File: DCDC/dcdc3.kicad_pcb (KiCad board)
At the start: 2 copper layers, 90 x 90 mm, 83 parts, among them M1-1 30V 60A, M1-2 30V 60A, M1-3 30V 60A, M2-1 30V 35A, M2-2 30V 35A, M2-3 30V 35A

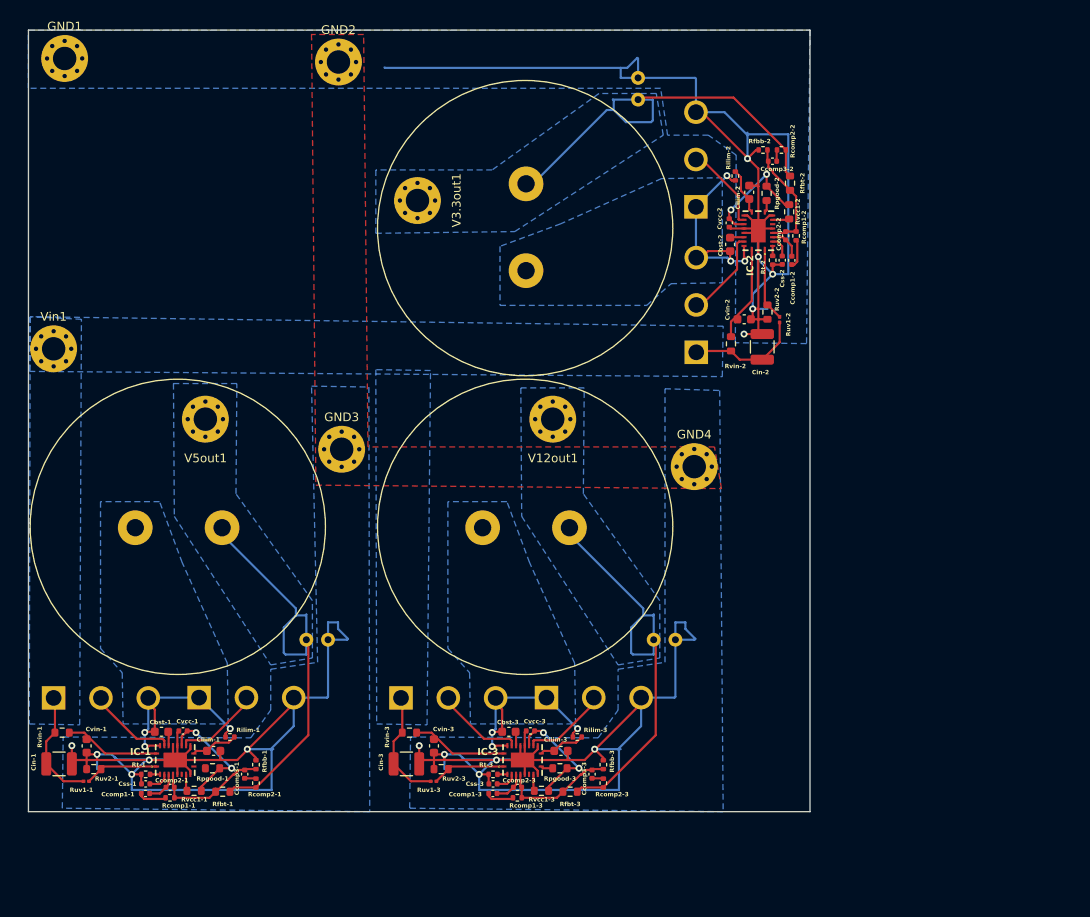
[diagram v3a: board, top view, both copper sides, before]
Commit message: pcb designed for 3 outputs
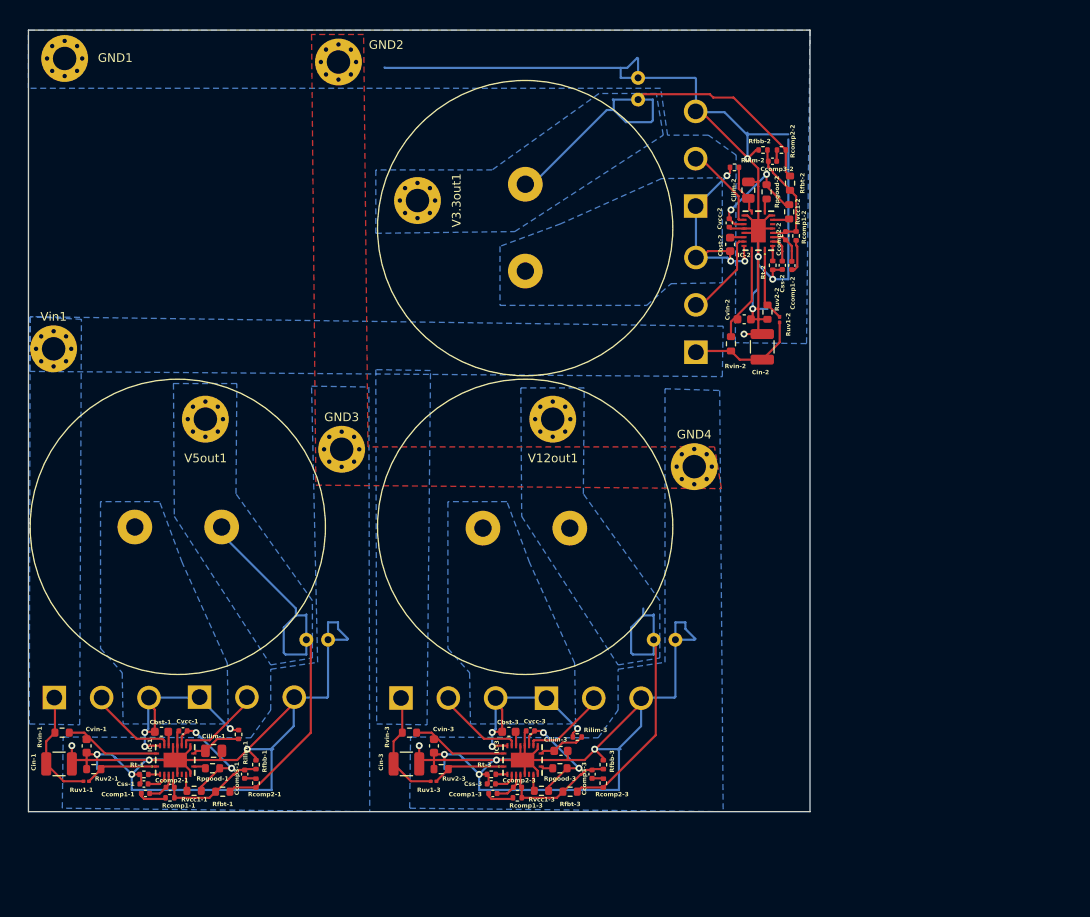
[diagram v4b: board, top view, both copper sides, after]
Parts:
- Ccomp1-1, Ccomp1-2: value 15 nF -> 8.2n
- Ccomp2-1: value 1.2 n -> 820p
- Ccomp2-2: value 1.2 n -> 1 n
- Ccomp3-1: value 910 p -> 470 p
- Ccomp3-2: value 910 p -> 330p
- Cilim-1, Cilim-2: value 10 p -> 5.1p; footprint Capacitor_SMD:C_0603_1608Metric -> Capacitor_SMD:C_0805_2012Metric
- Cout-1, Cout-2: value 56 u -> 10u
- L1-1: value 4.7 u -> 3.3u
- L1-2: value 4.7 u -> 2.2u
- Rcomp1-1: value 1.78 k -> 1.54k
- Rcomp1-2: value 1.78 k -> 1.27k
- Rcomp2-1: value 1.82 k -> 162
- Rcomp2-2: value 1.82 k -> 237
- Rfbb-1: value 1.27 k -> 3.4k
- Rfbb-2: value 1.27 k -> 5.76k
- Rilim-1: value 619 -> 1.74k
- Rilim-2: value 619 -> 1.5k
- Rt-1, Rt-2: value 69.8k -> 39.2k
- moved Rilim-1 1.04 mm to (54.2, 121.1), turned to 90 degrees
- moved Rilim-2 1.00 mm to (111.3, 55.8), turned to 180 degrees
- moved Ccomp1-2 0.59 mm to (117.9, 67.1)
- moved Css-2 0.59 mm to (116.8, 67.1)
- moved Rt-2 0.59 mm to (115.7, 67.1)
- moved Cilim-2 0.26 mm to (112.9, 58.4)
- moved Css-1 0.20 mm to (43.3, 126.8)
- moved Rt-1 0.20 mm to (43.3, 125.7)
- moved Css-3 0.20 mm to (83.3, 126.8)
- moved Rt-3 0.20 mm to (83.3, 125.7)
- moved Rpgood-2 0.17 mm to (115.0, 58.6)
- moved M2-2 0.10 mm to (106.8, 60.3)
- moved L1-1 0.09 mm to (47.2, 97.2)
- moved L1-2 0.09 mm to (87.2, 62.8)
- moved M1-1 0.09 mm to (33.0, 116.9)
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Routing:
- net /12V/V12out: track 50.2 -> 37.0 mm
- net /12V/GND: track 381.1 -> 378.6 mm
- net Net-(IC-1-PGOOD): track 0.00 -> 1.41 mm
- net Net-(Ccomp1-2-Pad1): track 3.29 -> 4.07 mm
- net Net-(IC-2-SS/TRK): track 2.46 -> 3.05 mm
- net Net-(IC-2-RT): track 1.14 -> 1.73 mm
- net Net-(IC-2-COMP): track 3.80 -> 4.39 mm
- net Net-(IC-1-ILIM): track 5.45 -> 6.02 mm

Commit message: one module of the dcdc converter seems ready again...
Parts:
- removed Cbst-2, Cbst-3: 100 n, Capacitor_SMD:C_0603_1608Metric
- removed Ccomp1-2: 8.2n, Capacitor_SMD:C_0402_1005Metric
- removed Ccomp1-3: 15 nF, Capacitor_SMD:C_0402_1005Metric
- removed Ccomp2-2: 1 n, Capacitor_SMD:C_0402_1005Metric
- removed Ccomp2-3: 1.2 n, Capacitor_SMD:C_0402_1005Metric
- removed Ccomp3-2: 330p, Capacitor_SMD:C_0402_1005Metric
- removed Ccomp3-3: 910 p, Capacitor_SMD:C_0402_1005Metric
- removed Cilim-2: 5.1p, Capacitor_SMD:C_0805_2012Metric
- removed Cilim-3: 10 p, Capacitor_SMD:C_0603_1608Metric
- removed Cin-2, Cin-3: 4.7 uF, Capacitor_SMD:C_1210_3225Metric
- removed Cout-2: 10u, Capacitor_THT:C_Radial_D6.3mm_H5.0mm_P2.50mm
- removed Cout-3: 56 u, Capacitor_THT:C_Radial_D6.3mm_H5.0mm_P2.50mm
- removed Css-2, Css-3: 56n, Capacitor_SMD:C_0402_1005Metric
- removed Cvcc-2, Cvcc-3: 2.2 u, Capacitor_SMD:C_0402_1005Metric
- removed Cvin-2, Cvin-3: 100 nF, Capacitor_SMD:C_0603_1608Metric
- removed GND2, GND3, GND4, V12out1, V3.3out1: ~, MountingHole:MountingHole_2.7mm_M2.5_Pad_Via
- removed IC-1, IC-2, IC-3: LM5145RGYR, Library:RGY0020B
- removed L1-2: 2.2u, Library:A3mmCoil
- removed L1-3: 4.7 u, Library:A3mmCoil
- removed M1-2, M1-3: 30V 60A, Library:TO545P521X1594X2566-3P
- removed M2-2, M2-3: 30V 35A, Library:TO545P521X1594X2566-3P
- removed Rcomp1-2: 1.27k, Resistor_SMD:R_0402_1005Metric
- removed Rcomp1-3: 1.78 k, Resistor_SMD:R_0402_1005Metric
- removed Rcomp2-2: 237, Resistor_SMD:R_0402_1005Metric
- removed Rcomp2-3: 1.82 k, Resistor_SMD:R_0402_1005Metric
- removed Rfbb-2: 5.76k, Resistor_SMD:R_0402_1005Metric
- removed Rfbb-3: 1.27 k, Resistor_SMD:R_0402_1005Metric
- removed Rfbt-2, Rfbt-3: 18 k, Resistor_SMD:R_0603_1608Metric
- removed Rilim-2: 1.5k, Resistor_SMD:R_0402_1005Metric
- removed Rilim-3: 619, Resistor_SMD:R_0402_1005Metric
- removed Rpgood-2, Rpgood-3, Rvcc1-2, Rvcc1-3: 20 k, Resistor_SMD:R_0603_1608Metric
- removed Rt-2: 39.2k, Resistor_SMD:R_0402_1005Metric
- removed Rt-3: 69.8k, Resistor_SMD:R_0402_1005Metric
- removed Ruv1-2, Ruv1-3: 68.1k, Resistor_SMD:R_0201_0603Metric
- removed Ruv2-2, Ruv2-3: 9.1 k, Resistor_SMD:R_0603_1608Metric
- removed Rvin-2, Rvin-3: 2.1, Resistor_SMD:R_0603_1608Metric
- removed Vin1: 12.5-22V, MountingHole:MountingHole_2.7mm_M2.5_Pad_Via
- added U1: LM5145RGYR, Library:RGY0020B, F.Cu at (76.5, 135.1)
- moved GND1 86.9 mm to (95.4, 104.9)
- moved Ccomp1-1 41.0 mm to (82.9, 139.3), turned to 180 degrees
- moved V5out1 40.5 mm to (85.5, 105.0)
- moved Cilim-1 38.0 mm to (88.3, 131.6)
- moved Rvin-1 38.0 mm to (69.9, 132.9)
- moved Rcomp1-1 37.8 mm to (82.8, 138.1), turned to 0 degrees
- moved Cout-1 37.2 mm to (97.7, 120.8), turned to 180 degrees
- moved Cvin-1 35.6 mm to (70.2, 134.5), turned to 0 degrees
- moved Ruv1-1 35.3 mm to (70.6, 135.9)
- moved Rfbt-1 35.2 mm to (87.1, 133.9)
- moved Cin-1 35.0 mm to (66.6, 135.8), turned to -90 degrees
- moved Ruv2-1 34.4 mm to (69.2, 138.4), turned to -90 degrees
- moved L1-1 34.3 mm to (78.0, 112.5)
- moved Rcomp2-1 33.3 mm to (87.9, 137.1), turned to -90 degrees
- moved Rpgood-1 33.1 mm to (82.6, 135.4), turned to -90 degrees
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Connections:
- Cbst-1 pad 2: Net-(IC-1-SW) -> Net-(U1-SW)
- L1-1 pad 1: Net-(IC-1-SW) -> Net-(U1-SW)
- M1-1 pad 1: /12V/Vin -> Net-(U1-HO)
- M1-1 pad 2: Net-(IC-1-HO) -> /12V/Vin
- M1-1 pad 3: Net-(IC-1-SW) -> Net-(U1-SW)
- M2-1 pad 1: Net-(IC-1-SW) -> Net-(U1-LO)
- M2-1 pad 2: Net-(IC-1-LO) -> Net-(U1-SW)
- Rilim-1 pad 2: Net-(IC-1-SW) -> Net-(U1-SW)
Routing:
- net /12V/GND: track 378.6 -> 70.2 mm, vias 15 -> 4
- net /3.3V/V3.3out: track 50.5 -> 0.00 mm
- net Net-(U1-SW): track 0.00 -> 46.4 mm
- net /12V/V12out: track 37.0 -> 0.00 mm
- net Net-(IC-3-SW): track 24.3 -> 0.00 mm, vias 3 -> 0
- net Net-(IC-2-SW): track 24.2 -> 0.00 mm, vias 3 -> 0
- net Net-(IC-1-SW): track 24.1 -> 0.00 mm, vias 3 -> 0
- net Net-(U1-HO): track 0.00 -> 18.6 mm, vias 0 -> 3
- net Net-(IC-2-FB): track 13.9 -> 0.00 mm
- net Net-(IC-3-FB): track 13.9 -> 0.00 mm
- net Net-(IC-2-VCC): track 13.5 -> 0.00 mm, vias 2 -> 0
- net Net-(IC-3-VCC): track 13.5 -> 0.00 mm, vias 2 -> 0
- net Net-(M1-3-D): track 13.2 -> 0.00 mm
- net /12V/Vin: track 26.4 -> 14.8 mm
- net Net-(IC-3-VIN): track 11.0 -> 0.00 mm
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- added copper zone on F.Cu, net /12V/Vin
- added copper zone on F.Cu, net /5V/V5out
- added copper zone on F.Cu, net Net-(U1-SW)
- removed copper zone on B.Cu, net /12V/V12out
- removed copper zone on B.Cu, net /12V/Vin
- removed copper zone on B.Cu, net /3.3V/V3.3out
- removed copper zone on B.Cu, net /5V/V5out
- removed copper zone on B.Cu, net Net-(IC-1-SW)
- removed copper zone on B.Cu, net Net-(IC-2-SW)
- removed copper zone on B.Cu, net Net-(IC-3-SW)
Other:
- board size 90 x 90 mm -> 40 x 40 mm

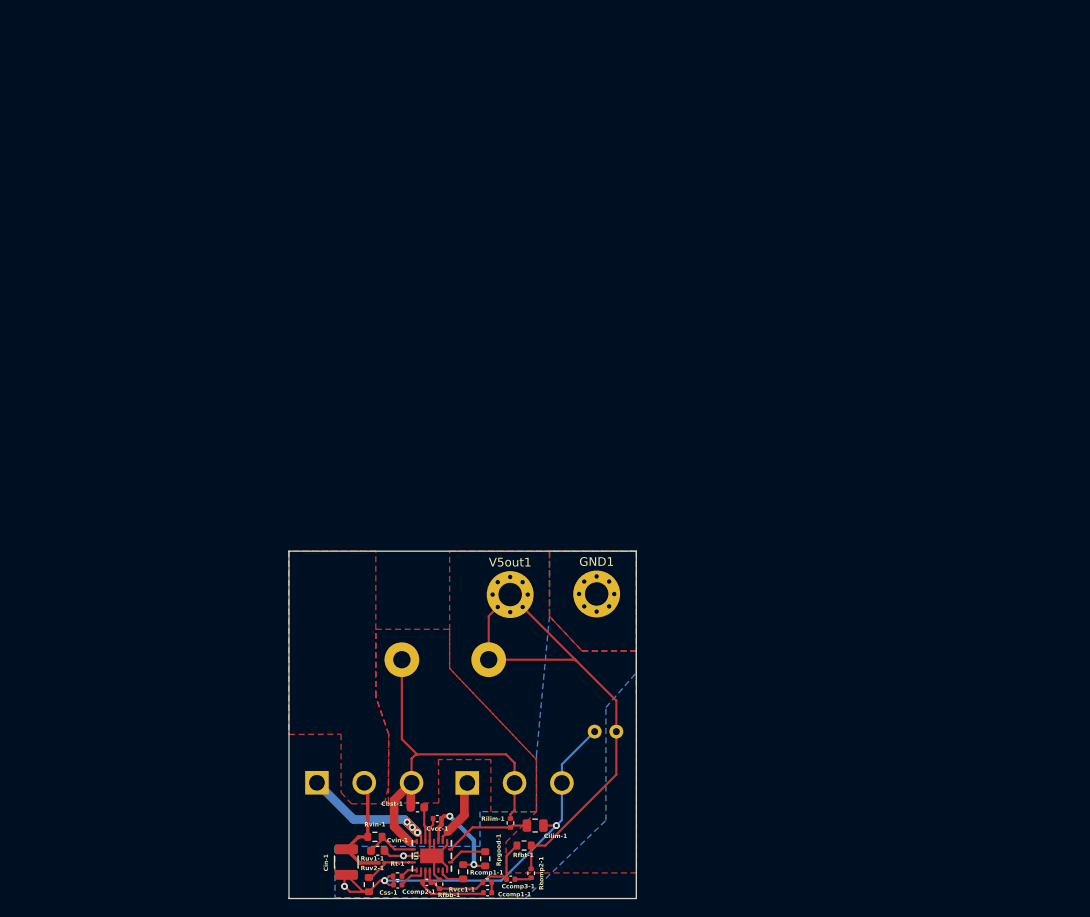
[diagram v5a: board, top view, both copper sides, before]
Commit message: 3 modules of DCDC, hinge
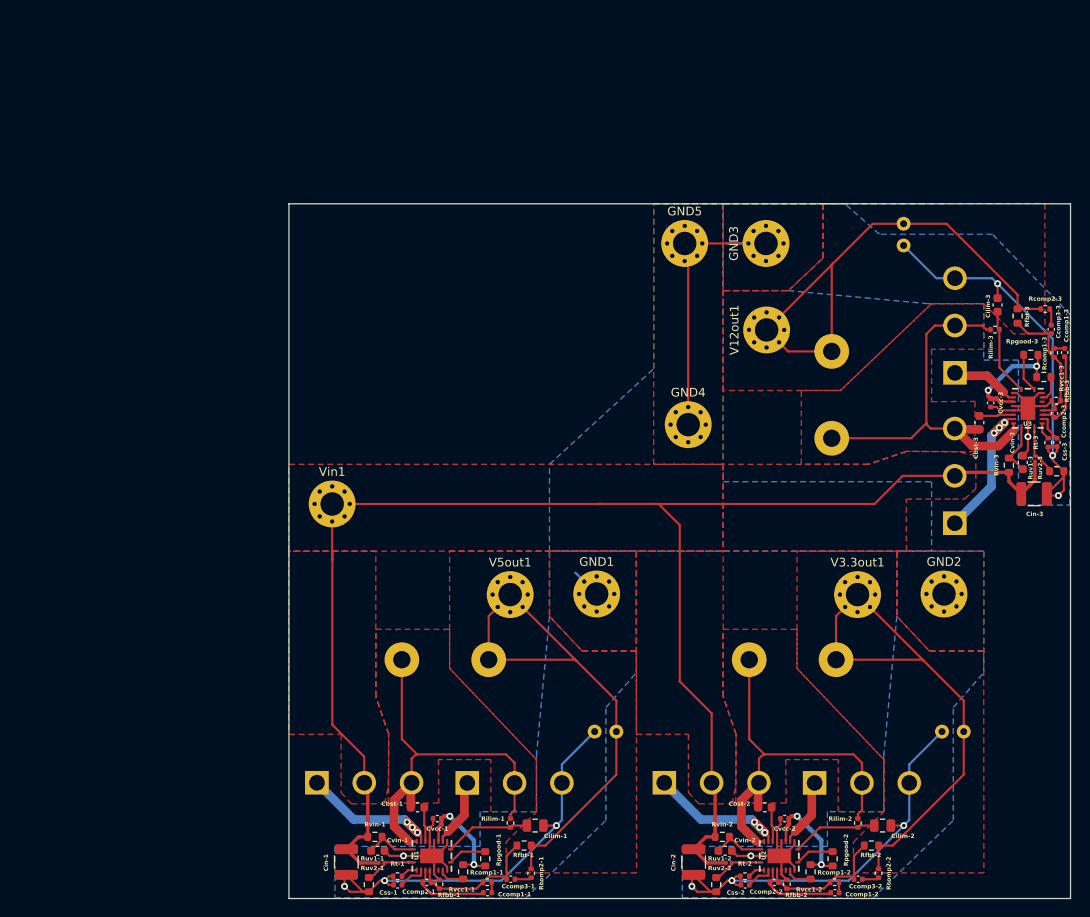
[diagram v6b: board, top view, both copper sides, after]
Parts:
- added Cbst-2: 100 n, Capacitor_SMD:C_0603_1608Metric, F.Cu at (114.8, 129.5)
- added Cbst-3: 100 n, Capacitor_SMD:C_0603_1608Metric, F.Cu at (139.5, 85.2)
- added Ccomp1-2: 8.2n, Capacitor_SMD:C_0402_1005Metric, F.Cu at (122.9, 139.3)
- added Ccomp1-3: 15 nF, Capacitor_SMD:C_0402_1005Metric, F.Cu at (149.3, 77.1)
- added Ccomp2-2: 1 n, Capacitor_SMD:C_0402_1005Metric, F.Cu at (115.9, 138.1)
- added Ccomp2-3: 1.2 n, Capacitor_SMD:C_0402_1005Metric, F.Cu at (148.1, 84.1)
- added Ccomp3-2: 330p, Capacitor_SMD:C_0402_1005Metric, F.Cu at (125.5, 137.8)
- added Ccomp3-3: 910 p, Capacitor_SMD:C_0402_1005Metric, F.Cu at (147.8, 74.5)
- added Cilim-2: 5.1p, Capacitor_SMD:C_0805_2012Metric, F.Cu at (128.3, 131.6)
- added Cilim-3: 10 p, Capacitor_SMD:C_0603_1608Metric, F.Cu at (141.6, 71.7)
- added Cin-2: 4.7 uF, Capacitor_SMD:C_1210_3225Metric, F.Cu at (106.6, 135.8)
- added Cin-3: 4.7 uF, Capacitor_SMD:C_1210_3225Metric, F.Cu at (145.8, 93.4)
- added Cout-2: 10u, Capacitor_THT:C_Radial_D6.3mm_H5.0mm_P2.50mm, B.Cu at (137.7, 120.8)
- added Cout-3: 56 u, Capacitor_THT:C_Radial_D6.3mm_H5.0mm_P2.50mm, B.Cu at (130.8, 62.3)
- added Css-2: 56n, Capacitor_SMD:C_0402_1005Metric, F.Cu at (112.5, 138.4)
- added Css-3: 56n, Capacitor_SMD:C_0402_1005Metric, F.Cu at (148.4, 87.5)
- added Cvcc-2: 2.2 u, Capacitor_SMD:C_0402_1005Metric, F.Cu at (117.1, 130.8)
- added Cvcc-3: 2.2 u, Capacitor_SMD:C_0402_1005Metric, F.Cu at (140.8, 82.9)
- added Cvin-2: 100 nF, Capacitor_SMD:C_0603_1608Metric, F.Cu at (110.2, 134.5)
- added Cvin-3: 100 nF, Capacitor_SMD:C_0603_1608Metric, F.Cu at (144.5, 89.8)
- added GND2: ~, MountingHole:MountingHole_2.7mm_M2.5_Pad_Via, F.Cu at (135.4, 104.9)
- added GND3: ~, MountingHole:MountingHole_2.7mm_M2.5_Pad_Via, F.Cu at (114.9, 64.6)
- added GND4: ~, MountingHole:MountingHole_2.7mm_M2.5_Pad_Via, F.Cu at (106.0, 85.4)
- added GND5: ~, MountingHole:MountingHole_2.7mm_M2.5_Pad_Via, F.Cu at (105.6, 64.6)
- added L1-2: 2.2u, Library:A3mmCoil, B.Cu at (118.0, 112.5)
- added L1-3: 4.7 u, Library:A3mmCoil, B.Cu at (122.5, 82.0)
- added M1-2: 30V 60A, Library:TO545P521X1594X2566-3P, B.Cu at (103.2, 126.7)
- added M1-3: 30V 60A, Library:TO545P521X1594X2566-3P, B.Cu at (136.7, 96.8)
- added M2-2: 30V 35A, Library:TO545P521X1594X2566-3P, B.Cu at (120.5, 126.7)
- added M2-3: 30V 35A, Library:TO545P521X1594X2566-3P, B.Cu at (136.7, 79.5)
- added Rcomp1-2: 1.27k, Resistor_SMD:R_0402_1005Metric, F.Cu at (122.8, 138.1)
- added Rcomp1-3: 1.78 k, Resistor_SMD:R_0402_1005Metric, F.Cu at (148.1, 77.2)
- added Rcomp2-2: 237, Resistor_SMD:R_0402_1005Metric, F.Cu at (127.9, 137.1)
- added Rcomp2-3: 1.82 k, Resistor_SMD:R_0402_1005Metric, F.Cu at (147.1, 72.1)
- added Rfbb-2: 5.76k, Resistor_SMD:R_0402_1005Metric, F.Cu at (117.3, 138.3)
- added Rfbb-3: 1.27 k, Resistor_SMD:R_0402_1005Metric, F.Cu at (148.3, 82.7)
- added Rfbt-2: 18 k, Resistor_SMD:R_0603_1608Metric, F.Cu at (127.1, 133.9)
- added Rfbt-3: 18 k, Resistor_SMD:R_0603_1608Metric, F.Cu at (143.9, 72.9)
- added Rilim-2: 1.5k, Resistor_SMD:R_0402_1005Metric, F.Cu at (125.5, 131.3)
- added Rilim-3: 619, Resistor_SMD:R_0402_1005Metric, F.Cu at (141.3, 74.5)
- added Rpgood-2: 20 k, Resistor_SMD:R_0603_1608Metric, F.Cu at (122.6, 135.4)
- added Rpgood-3: 20 k, Resistor_SMD:R_0603_1608Metric, F.Cu at (145.4, 77.4)
- added Rt-2: 39.2k, Resistor_SMD:R_0402_1005Metric, F.Cu at (112.5, 137.4)
- added Rt-3: 69.8k, Resistor_SMD:R_0402_1005Metric, F.Cu at (147.4, 87.5)
- added Ruv1-2: 68.1k, Resistor_SMD:R_0201_0603Metric, F.Cu at (110.6, 135.9)
- added Ruv1-3: 68.1k, Resistor_SMD:R_0201_0603Metric, F.Cu at (145.9, 89.4)
- added Ruv2-2: 9.1 k, Resistor_SMD:R_0603_1608Metric, F.Cu at (109.2, 138.4)
- added Ruv2-3: 9.1 k, Resistor_SMD:R_0603_1608Metric, F.Cu at (148.4, 90.8)
- added Rvcc1-2: 20 k, Resistor_SMD:R_0603_1608Metric, F.Cu at (120.1, 136.9)
- added Rvcc1-3: 20 k, Resistor_SMD:R_0603_1608Metric, F.Cu at (146.9, 79.9)
- added Rvin-2: 2.1, Resistor_SMD:R_0603_1608Metric, F.Cu at (109.9, 132.9)
- added Rvin-3: 2.1, Resistor_SMD:R_0603_1608Metric, F.Cu at (142.9, 90.1)
- added U2: LM5145RGYR, Library:RGY0020B, F.Cu at (116.5, 135.1)
- added U3: LM5145RGYR, Library:RGY0020B, F.Cu at (145.1, 83.5)
- added V12out1: ~, MountingHole:MountingHole_2.7mm_M2.5_Pad_Via, F.Cu at (115.0, 74.5)
- added V3.3out1: ~, MountingHole:MountingHole_2.7mm_M2.5_Pad_Via, F.Cu at (125.5, 105.0)
- added Vin1: 12.5-22V, MountingHole:MountingHole_2.7mm_M2.5_Pad_Via, F.Cu at (65.0, 94.6)
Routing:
- net /12V/Vin: track 14.8 -> 194.7 mm
- net /12V/GND: track 70.2 -> 249.0 mm, vias 4 -> 12
- net /12V/V12out: track 0.00 -> 60.4 mm
- net /3.3V/V3.3out: track 0.00 -> 60.4 mm
- net Net-(U3-SW): track 0.00 -> 46.4 mm
- net Net-(U2-SW): track 0.00 -> 46.4 mm
- net Net-(U3-HO): track 0.00 -> 18.6 mm, vias 0 -> 3
- net Net-(U2-HO): track 0.00 -> 18.6 mm, vias 0 -> 3
- net Net-(U3-FB): track 0.00 -> 15.6 mm
- net Net-(U2-FB): track 0.00 -> 15.6 mm
- net Net-(U3-VCC): track 0.00 -> 13.6 mm, vias 0 -> 2
- net Net-(U2-VCC): track 0.00 -> 13.6 mm, vias 0 -> 2
- net Net-(U3-ILIM): track 0.00 -> 9.95 mm
- net Net-(U2-ILIM): track 0.00 -> 9.95 mm
- net Net-(U3-COMP): track 0.00 -> 9.79 mm
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- added copper zone on F.Cu, net /12V/V12out
- added copper zone on F.Cu, net /3.3V/V3.3out
- added copper zone on F.Cu, net Net-(U2-SW)
- added copper zone on F.Cu, net Net-(U3-SW)
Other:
- board size 40 x 40 mm -> 90 x 80 mm
